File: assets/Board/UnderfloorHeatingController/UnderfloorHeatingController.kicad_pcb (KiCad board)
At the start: 2 copper layers, 141.5 x 70.4 mm, 63 parts, among them J1 Screw_Terminal_01x02, J10 Screw_Terminal_01x02, J11 Screw_Terminal_01x02, J12 Screw_Terminal_01x02, J13 Screw_Terminal_01x02, J14 Screw_Terminal_01x02, J2 Screw_Terminal_01x03, J3 Screw_Terminal_01x03, J4 Screw_Terminal_01x02, J5 Screw_Terminal_01x02, J6 Screw_Terminal_01x02, J7 Screw_Terminal_01x02, J8 Screw_Terminal_01x02, J9 Screw_Terminal_01x02, K1 Relay_SPST_Latching_1coil, K2 Relay_SPST_Latching_1coil, K3 Relay_SPST_Latching_1coil, K4 Relay_SPST_Latching_1coil, K5 Relay_SPST_Latching_1coil, K6 Relay_SPST_Latching_1coil, K7 Relay_SPST_Latching_1coil, U1 BL0937B, U2 Waveshare_ESP32-S3-Tiny, U3 DRV8833PWR, U4 DRV8833PWR, U5 DRV8833PWR, U6 DRV8833PWR

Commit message: Improved routing and layout.
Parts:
- C5: value 0.1µF -> 0.1uF
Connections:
- J10 pad 1: /ETA relays/Relay pair - ETA2/POWER_RELAY_B -> /ETA relays/Relay pair - ETA3/POWER_RELAY_A
- J11 pad 1: /ETA relays/Relay pair - ETA3/POWER_RELAY_A -> /ETA relays/Relay pair - ETA3/POWER_RELAY_B
- J13 pad 1: /ETA relays/Relay pair - ETA3/POWER_RELAY_A -> /ETA relays/Relay pair - ETA3/POWER_RELAY_B
- J2 pad 1: POWER_PE -> POWER_L_UNFUSED
- J2 pad 2: POWER_L_UNFUSED -> POWER_PE
- J3 pad 2: POWER_N_MON -> POWER_PE
- J3 pad 3: POWER_PE -> POWER_N_MON
- J4 pad 1: /ETA relays/Relay pair - ETA1/POWER_RELAY_B -> /ETA relays/Relay pair - ETA1/POWER_RELAY_A
- J6 pad 1: /ETA relays/Relay pair - ETA1/POWER_RELAY_B -> /ETA relays/Relay pair - ETA1/POWER_RELAY_A
- J8 pad 1: /ETA relays/Relay pair - ETA2/POWER_RELAY_A -> /ETA relays/Relay pair - ETA1/POWER_RELAY_B
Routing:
- net /ETA relays/Relay pair - ETA3/POWER_RELAY_A: track 45.3 -> 23.5 mm
- net /ETA relays/Relay pair - ETA1/POWER_RELAY_B: track 42.8 -> 23.6 mm
- net /ETA relays/Relay pair - ETA1/POWER_RELAY_A: track 22.2 -> 38.7 mm
- net POWER_L: track 285.8 -> 269.4 mm
- net /ETA relays/Relay pair - ETA2/POWER_RELAY_B: track 25.1 -> 11.0 mm
- net /ETA relays/Relay pair - ETA3/POWER_RELAY_B: track 28.1 -> 38.9 mm
- net POWER_PE: track 48.8 -> 58.9 mm
- net /ETA relays/Relay pair - ETA2/POWER_RELAY_A: track 23.3 -> 13.4 mm
- net POWER_N_MON: track 319.7 -> 310.8 mm
- net POWER_L_UNFUSED: track 19.3 -> 18.3 mm

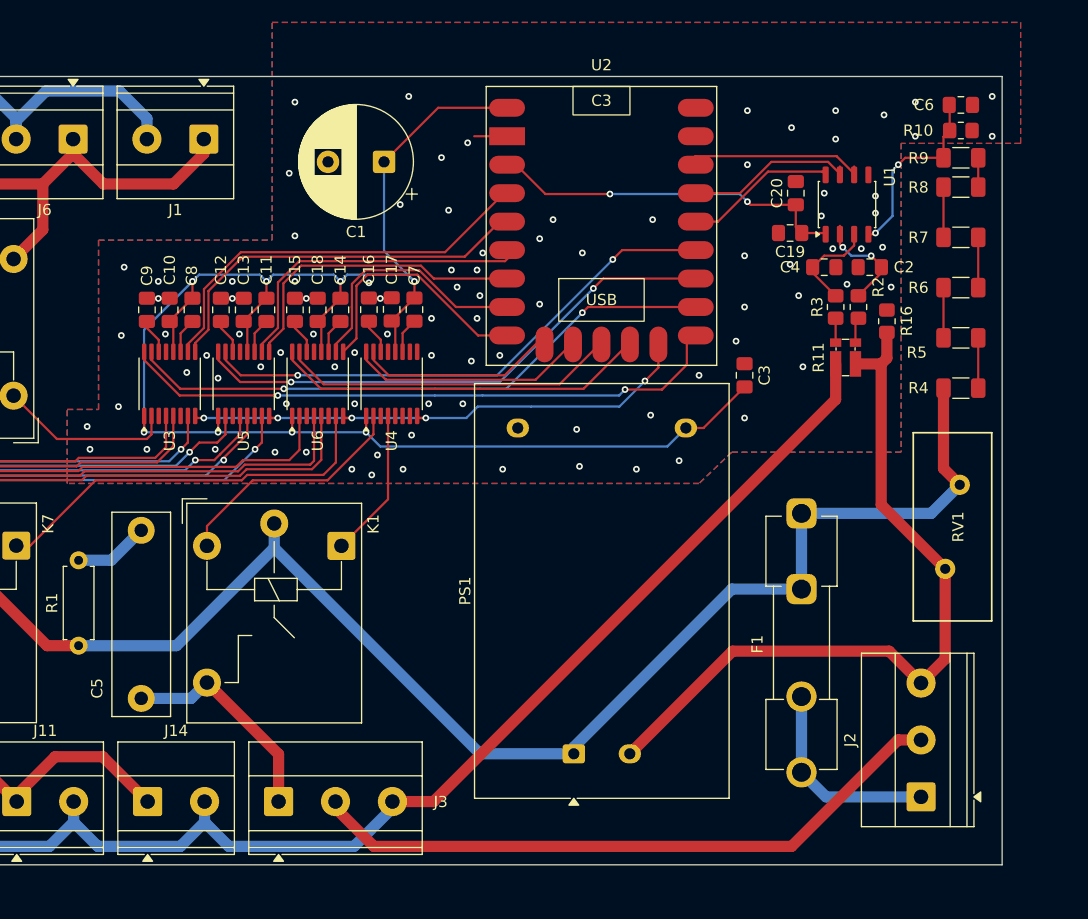
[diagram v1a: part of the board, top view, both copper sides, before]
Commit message: Corrected current monitor lines.
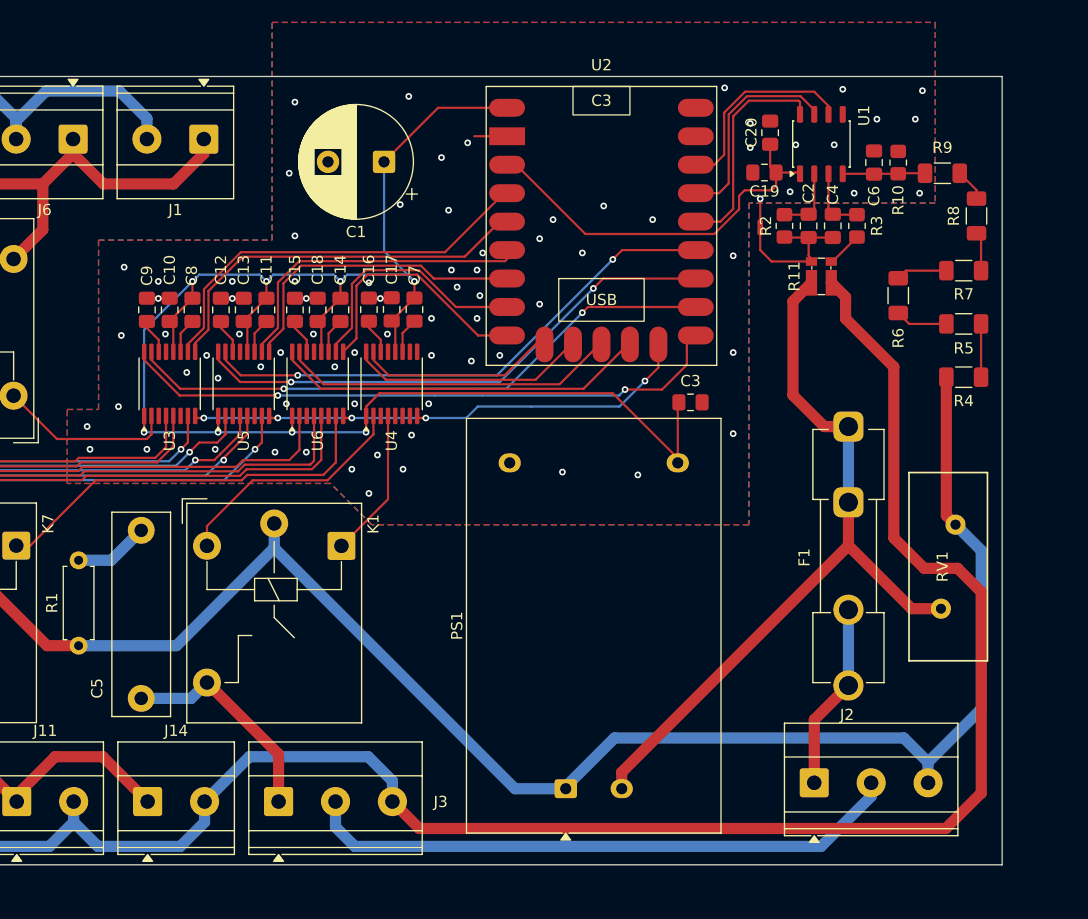
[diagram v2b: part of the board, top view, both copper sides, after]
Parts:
- removed R16: 0, Resistor_SMD:R_0805_2012Metric_Pad1.20x1.40mm_HandSolder
- added NT1: NetTie_2, NetTie:NetTie-2_SMD_Pad0.5mm, F.Cu at (156.3, 52.6)
- moved RV1 11.2 mm to (172.5, 86.6), turned to 90 degrees
- moved R2 9.80 mm to (158.5, 52.5)
- moved J2 9.61 mm to (161.2, 102.2), turned to 0 degrees
- moved C6 9.30 mm to (166.5, 46.8), turned to 90 degrees
- moved F1 8.81 mm to (164.2, 70.4)
- moved R11 7.55 mm to (161.8, 57.0)
- moved R3 7.49 mm to (165.0, 52.5)
- moved C2 6.59 mm to (160.7, 52.5), turned to -90 degrees
- moved R10 6.28 mm to (168.7, 46.8), turned to 90 degrees
- moved C20 5.86 mm to (157.2, 44.1)
- moved C19 5.86 mm to (156.7, 47.7)
- moved U1 5.86 mm to (161.8, 45.1)
- moved R6 5.63 mm to (168.7, 58.7), turned to 90 degrees
- moved C3 5.40 mm to (150.1, 68.2), turned to 0 degrees
- moved C4 3.76 mm to (162.8, 52.5), turned to 90 degrees
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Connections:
- net POWER_L_UNFUSED renamed POWER_N_UNFUSED
- C2 pad 2: GND -> HOT_GND
- C4 pad 1: GND -> HOT_GND
- F1 pad 1: POWER_L -> POWER_N
- J2 pad 3: POWER_N -> POWER_L
- R11 pad 1: POWER_N_MON -> POWER_N
- R11 pad 2: MON_CURRENT_SENSE_2 -> HOT_GND
- R11 pad 3: MON_CURRENT_SENSE_1 -> MON_CURRENT_SENSE_2
- R11 pad 4: POWER_N -> POWER_N_MON
- R2 pad 1: MON_CURRENT_SENSE_1 -> HOT_GND
- RV1 pad 1: POWER_L -> POWER_N
- RV1 pad 2: POWER_N -> POWER_L
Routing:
- net POWER_N_MON: track 310.8 -> 362.4 mm
- net POWER_L: track 269.4 -> 286.7 mm
- net HOT_GND: track 0.00 -> 13.3 mm
- net Net-(U1-VP): track 16.9 -> 7.39 mm, vias 2 -> 0
- net MON_SEL: track 14.4 -> 20.6 mm
- net POWER_PE: track 58.9 -> 54.4 mm
- net Net-(U1-IP): track 10.4 -> 6.00 mm, vias 2 -> 0
- net MON_CF1: track 16.1 -> 19.5 mm
- net +3V3: track 31.4 -> 34.4 mm, vias 2 -> 0
- net Net-(U1-IN): track 8.91 -> 5.95 mm
- net MON_CURRENT_SENSE_1: track 2.28 -> 0.00 mm
- net GND: track 3.74 -> 5.78 mm, vias 93 -> 78
- net POWER_N_UNFUSED: track 18.3 -> 16.7 mm
- net MON_CURRENT_SENSE_2: track 2.17 -> 3.19 mm
- net Net-(R7-Pad2): track 4.49 -> 3.50 mm
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
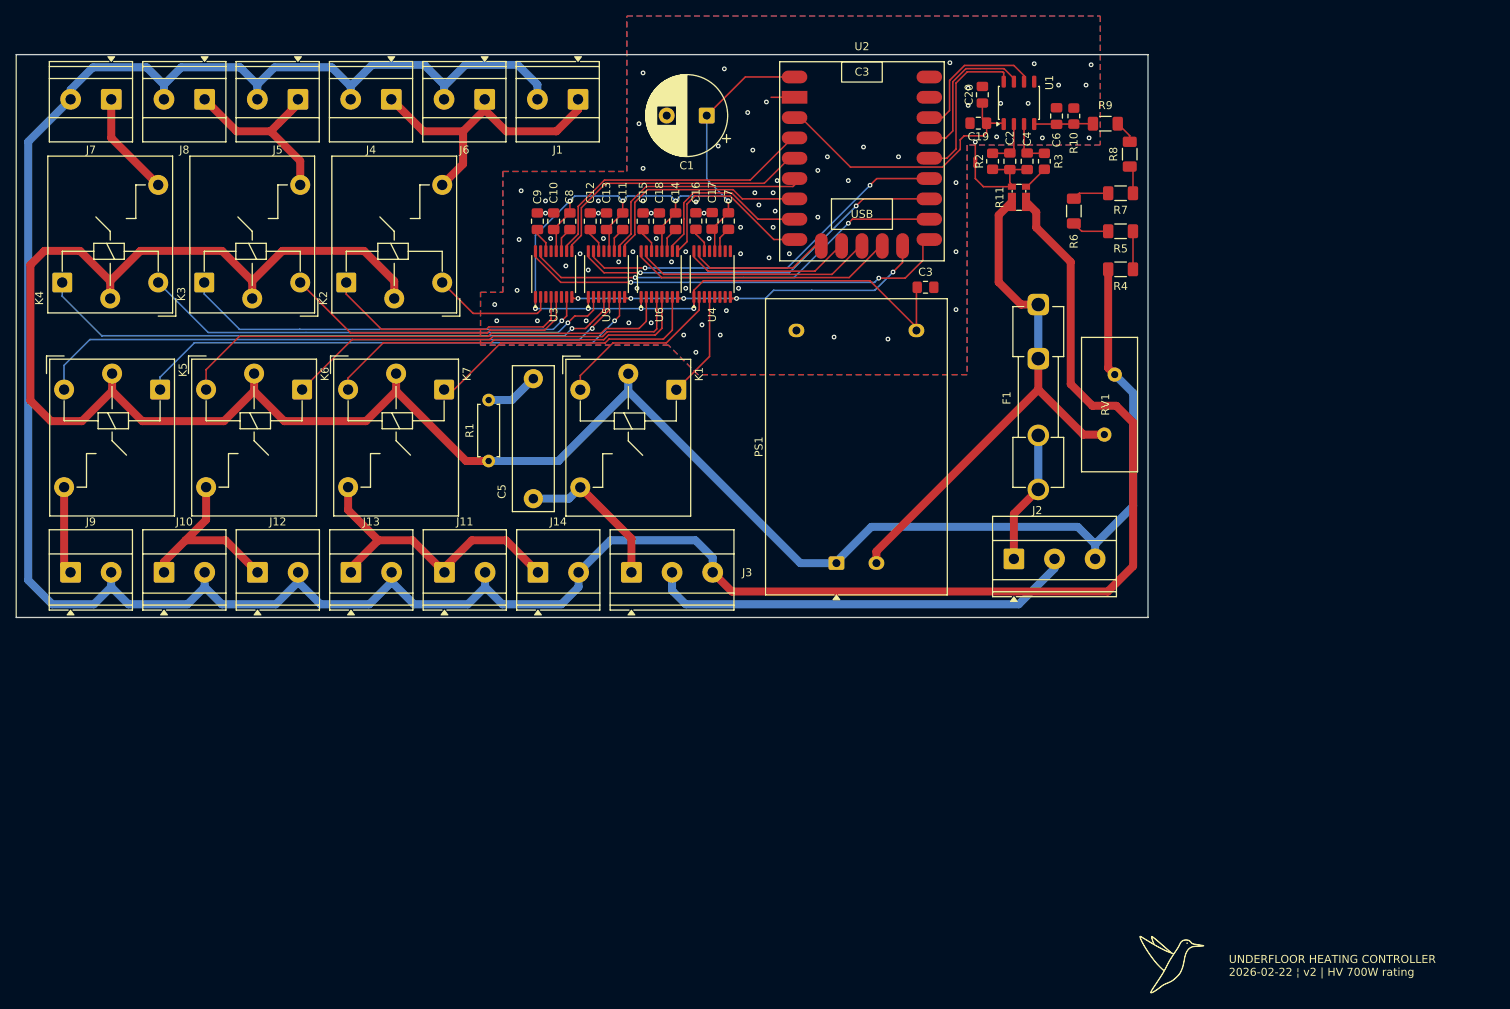
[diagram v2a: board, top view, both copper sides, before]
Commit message: Increased clearance.
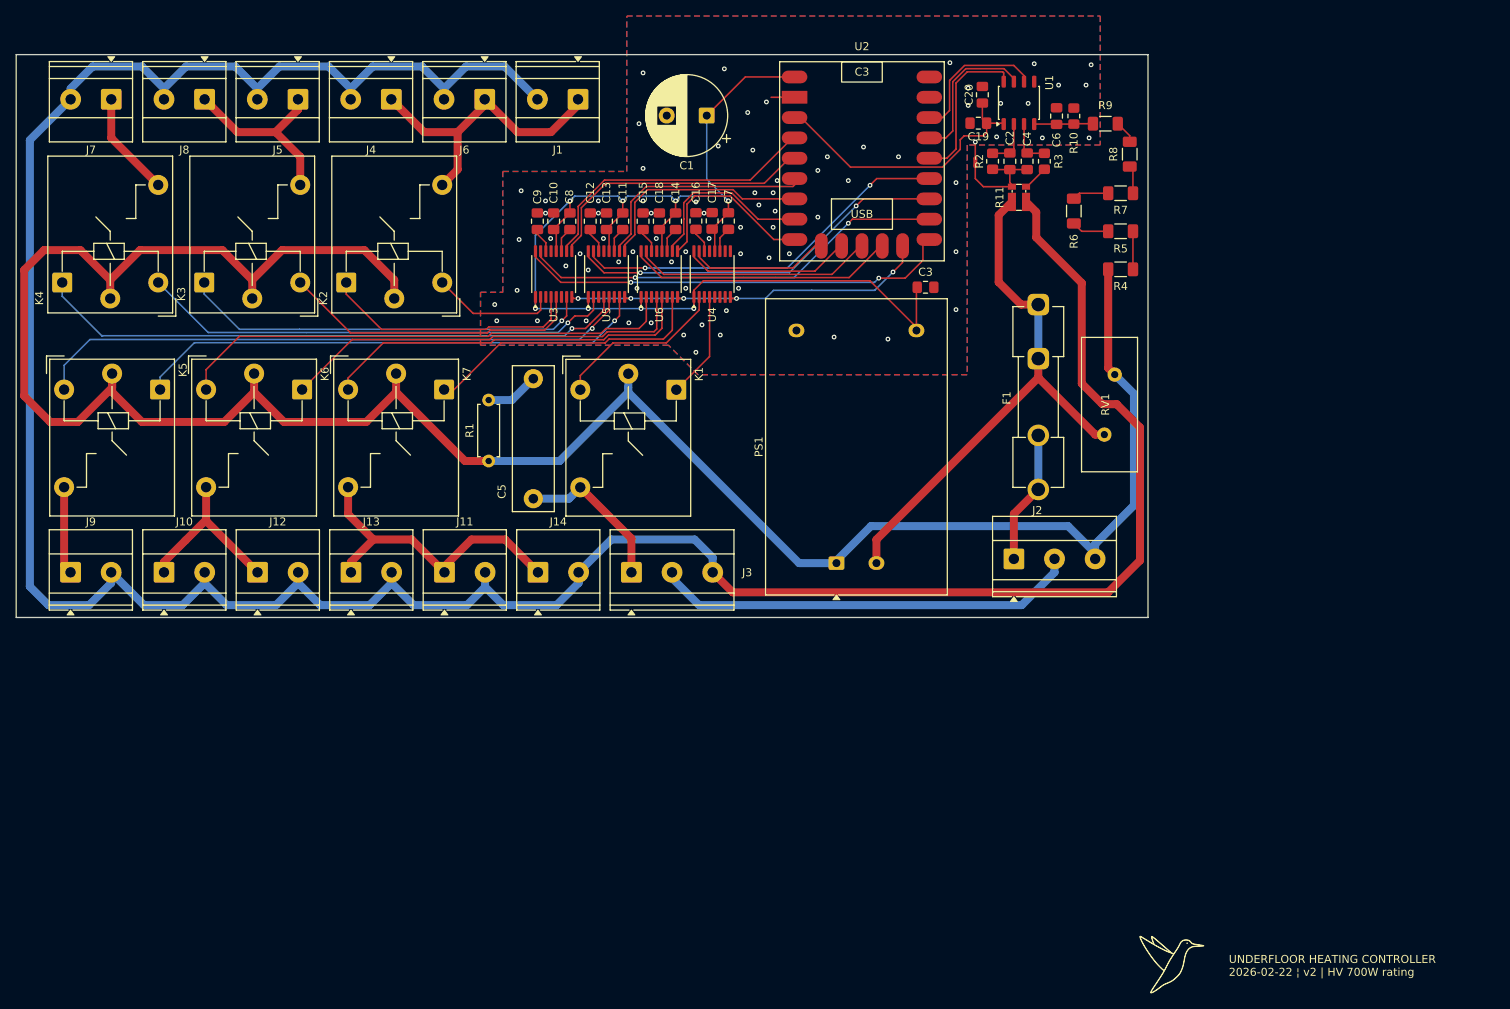
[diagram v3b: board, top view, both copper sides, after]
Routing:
- net POWER_L: track 286.7 -> 291.7 mm
- net POWER_N_MON: track 362.4 -> 360.2 mm
- net /ETA relays/Relay pair - ETA3/POWER_RELAY_A: track 23.5 -> 22.0 mm
- net POWER_N: track 68.5 -> 69.1 mm
- net POWER_PE: track 54.4 -> 53.9 mm
